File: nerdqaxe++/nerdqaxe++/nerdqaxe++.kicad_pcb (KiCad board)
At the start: 6 copper layers, 89 x 165 mm, 271 parts, among them J1 XT30, M1 Fan_4pin, M2 Fan_4pin, U10 CSD95472Q5MC, U19 BM1370_mode1, U2 TPSM82901SISR, U20 BM1370, U25 BM1370_mode1, U26 BM1370_mode1, U3 TPS53647, U30 T-Display-S3, U32 EMC2302-1, U33 TXU0102-DCU, U36 MCP1824T-1202E, U37 TMP1075, U38 TMP1075, U4 CSD95472Q5MC, U6 SN74AVC4T774, U7 MCP1824T-0802E, U8 25MHz, U9 CSD95472Q5MC

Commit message: Powermining revision
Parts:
- removed the ? at (132.5, 100.5)
- removed the ? at (57.5, 175.5)
- removed the ? at (56.0, 99.0)
- removed the ? at (134.0, 177.0)
- removed the ? at (132.5, 175.5)
- removed the ? at (134.0, 99.0)
- removed the ? at (56.0, 177.0)
- removed the ? at (58.5, 98.5)
- removed L5, L6: 220nH, myfootprints:IFLR-4031GC-01-8x10
- added ?: , , F.Cu at (123.0, 185.0)
- added ?: , , F.Cu at (57.5, 175.5)
- added ?: , , F.Cu at (132.5, 175.5)
- added ?: , , F.Cu at (67.0, 185.0)
- added ?: , , F.Cu at (57.5, 100.5)
- added ?: , , F.Cu at (132.5, 100.5)
- added ?: , , F.Cu at (67.0, 91.0)
- added ?: LOGO, LOGO, F.Cu at (55.9, 138.4)
- added ?: , , F.Cu at (123.0, 91.0)
- added F1: Fuseholder_Blade_Mini_Keystone_3568, Fuse:Fuseholder_Blade_Mini_Keystone_3568, F.Cu at (65.1, 42.0)
- added L2: 180nH, Powermining:PA5187-181HLT, F.Cu at (94.0, 65.9)
- added L3: 180nH, Powermining:PA5187-181HLT, F.Cu at (94.0, 76.6)
- L1: value 220nH -> 180nH; footprint myfootprints:IFLR-4031GC-01-8x10 -> Powermining:PA5187-181HLT
- moved G*** 1.37 mm to (133.9, 143.8)
- moved G*** 0.35 mm to (134.8, 114.4)
- moved G*** 0.35 mm to (134.9, 128.8)
- moved L1 0.06 mm to (94.0, 55.2)
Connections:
- J1 pad 1: +12V -> Net-(J1-+V)
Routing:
- net VDD: vias 227 -> 246
- net Net-(J1-+V): vias 0 -> 58
- net GND: vias 414 -> 566
- net +12V: vias 45 -> 63
- net (no net): vias 0 -> 1
- added copper zone on B.Cu, net +12V
- added copper zone on In1.Cu, net +12V
- added copper zone on In3.Cu, net +12V
- added copper zone on B.Cu, net Net-(J1-+V)
- added copper zone on F.Cu, net Net-(J1-+V)
- added copper zone on In1.Cu, net Net-(J1-+V)
- added copper zone on In2.Cu, net Net-(J1-+V)
- added copper zone on In3.Cu, net Net-(J1-+V)
- added copper zone on In4.Cu, net Net-(J1-+V)
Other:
- board text added: "rev6.1PM"
- board text removed: "4mm"
- board text removed: "5mm"
- board text removed: "rev6.1"

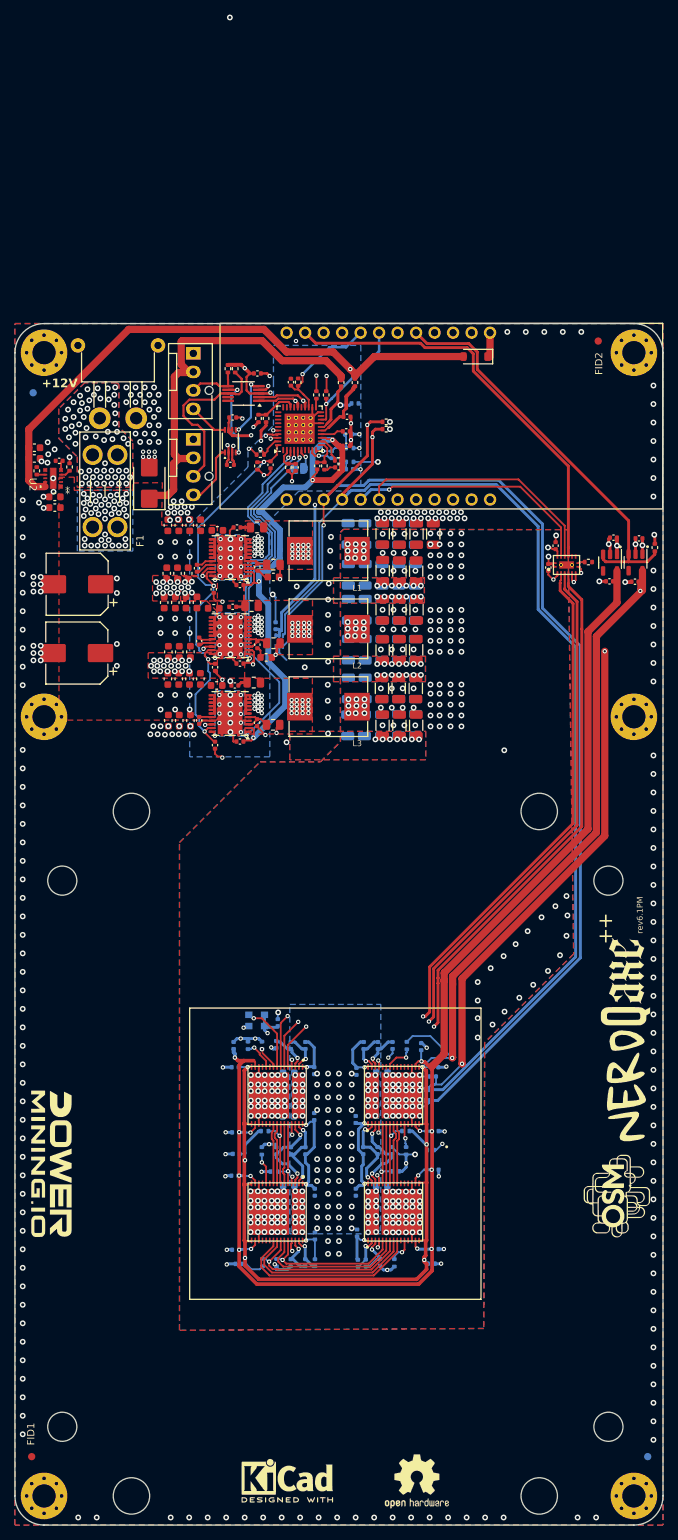
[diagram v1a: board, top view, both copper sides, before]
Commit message: Edit on rev 6.1PM
- Moved XT30 connector to the back of the board
- Edited VDD polygon
- Fixed various via placements
- Fixed various tracing
- Updated BM1370 footprint and solder paste stencil
- Updated CSD95472Q5MC footprint and solder paste stencil
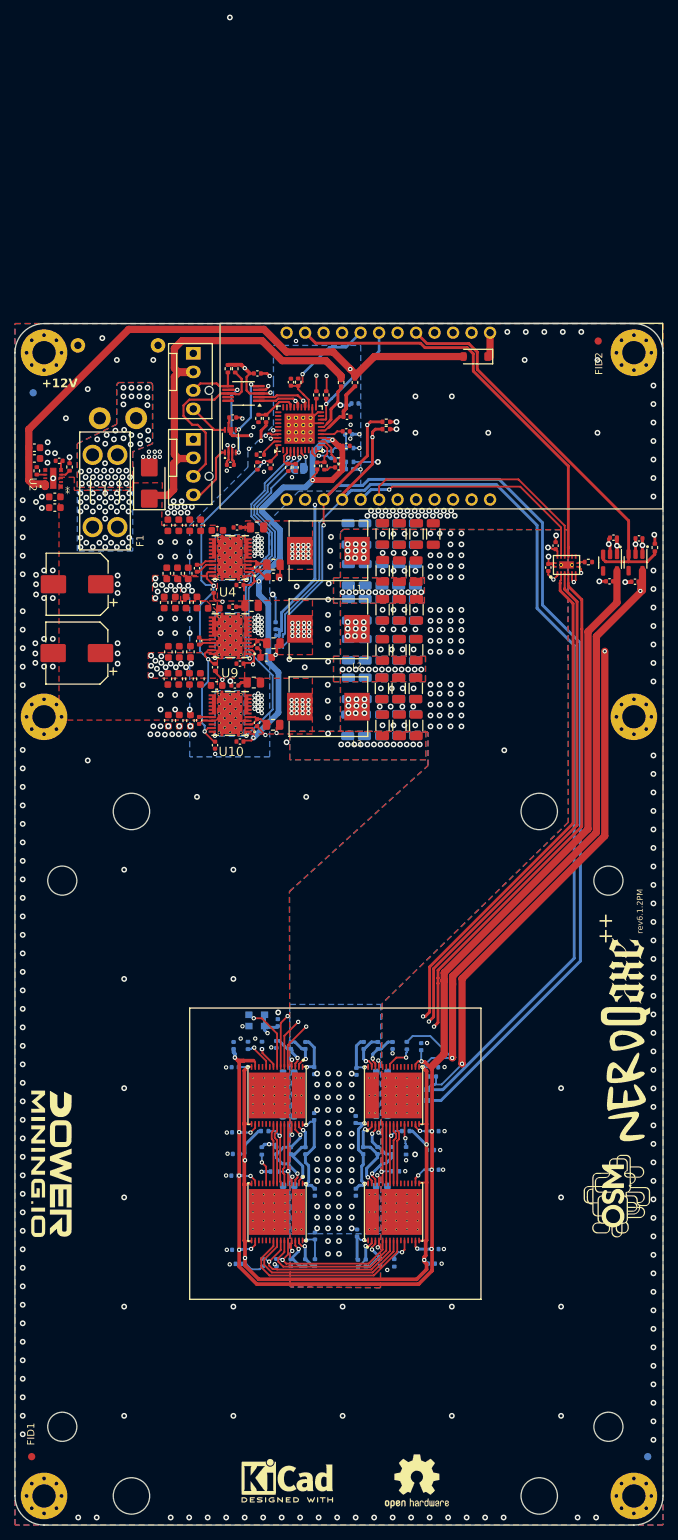
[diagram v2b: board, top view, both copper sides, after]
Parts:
- C149, C164, C18: value 1nF -> 2.7nF
- J1: moved to B.Cu
- U10, U4, U9: footprint myfootprints:CSD95472-SON-5x6 -> qaxe:CSD95472Q5MC
- U19, U25, U26: value BM1370_mode1 -> BM1370; footprint qaxe:BM1370 -> qaxe:BM1370_paste
- U20: footprint qaxe:BM1370 -> qaxe:BM1370_paste
- turned J1 to 180 degrees
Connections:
- R4 pad 2: /Power/FCCM -> Net-(U3-/SKIP-NVM)
- U10 pad 10: /Power/FCCM -> unconnected-(U10-FCCM-Pad10)
- U3 pad 39: /Power/FCCM -> Net-(U3-/SKIP-NVM)
- U4 pad 10: /Power/FCCM -> unconnected-(U4-FCCM-Pad10)
- U9 pad 10: /Power/FCCM -> unconnected-(U9-FCCM-Pad10)
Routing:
- net GND: track 187.5 -> 64.1 mm, vias 566 -> 383
- net /Power/FCCM: track 49.9 -> 0.00 mm, vias 4 -> 0
- net Net-(U3-/SKIP-NVM): track 0.00 -> 2.94 mm
- net /Power/TPS_CSP3: track 50.2 -> 47.7 mm
- net /Power/TPS_TSEN: track 60.2 -> 58.0 mm
- net +VRef: track 83.5 -> 81.4 mm
- net +3V3: track 120.3 -> 122.1 mm
- net /Power/TPS_CSP1: track 24.6 -> 22.9 mm
- net +12V: track 54.4 -> 56.1 mm, vias 63 -> 60
- net /Power/TPS_CSP2: track 36.4 -> 34.7 mm
- net +5V: track 155.1 -> 154.0 mm
- net /Power/TPS_PWM3: track 51.1 -> 50.4 mm
- net Net-(U9-VSW): track 0.50 -> 0.00 mm
- net Net-(U4-VSW): track 0.50 -> 0.00 mm
- net Net-(U10-VSW): track 0.50 -> 0.00 mm
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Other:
- board text added: "rev6.1.2PM"
- board text removed: "rev6.1PM"
